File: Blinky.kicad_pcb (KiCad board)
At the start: 2 copper layers, 170 x 83.6 mm, 42 parts, among them J1 DTF13-4P-G003, J2 DTF13-4P-G003, J3 1053091104, J4 2002411132, Q1 IPD90P03P404ATMA2, Q2 IPD90P03P404ATMA2, U1 DCM4623TD2J13D0T00, U2 DCM4623TD2J13D0T00, U3 TLP184, U4 LTV-817S

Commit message: Finished layout rev 1
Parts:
- F1, F2: value 0031.8201 -> 0031.8221; footprint Fuse:Fuseholder_Cylinder-5x20mm_Schurter_0031_8201_Horizontal_Open -> AERO_Fuses:Schurter 0031.8221
- moved D1 27.6 mm to (210.0, 79.4), turned to 90 degrees
- moved R1 27.4 mm to (213.7, 79.5), turned to 90 degrees
- moved R2 27.1 mm to (218.0, 107.8)
- moved D2 26.8 mm to (218.0, 104.3)
- moved F1 14.1 mm to (75.0, 108.6)
- moved F2 14.1 mm to (75.0, 72.0)
- moved R6 12.6 mm to (88.8, 59.4)
- moved C3 7.06 mm to (186.7, 114.6), turned to 90 degrees
- moved L4 6.00 mm to (198.2, 67.0)
- moved R8 6.00 mm to (198.2, 59.8)
- moved C6 5.41 mm to (186.7, 70.5)
- moved L3 4.84 mm to (88.8, 68.2)
- moved R11 3.70 mm to (155.7, 102.9)
- moved R9 3.60 mm to (155.8, 98.4), turned to -90 degrees
- moved C4 3.20 mm to (112.2, 62.9)
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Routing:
- net /Control Signals/INVERTER-: track 0.00 -> 247.3 mm, vias 0 -> 3
- net /Control Signals/HV_FAULT: track 0.00 -> 133.0 mm
- net /Control Signals/HV_EN: track 0.00 -> 129.4 mm
- net /Control Signals/~{LV_FAULT}: track 0.00 -> 57.5 mm, vias 0 -> 1
- net TSMS12V: track 0.00 -> 55.7 mm, vias 0 -> 1
- net /Control Signals/LV_EN: track 0.00 -> 53.2 mm, vias 0 -> 1
- net /VICOR-1/HV_TRIM: track 0.00 -> 32.8 mm, vias 0 -> 1
- net /VICOR-2/HV_TRIM: track 0.00 -> 31.2 mm
- net /TSV Connectors/INVERTER+: track 0.00 -> 30.1 mm, vias 0 -> 10
- net /VICOR-2/VICOR_RAW: track 18.9 -> 0.00 mm
- net /VICOR-1/VICOR_RAW: track 18.9 -> 0.00 mm
- net Net-(D3-A): track 0.00 -> 10.1 mm
- net Net-(D2-A): track 0.00 -> 9.55 mm, vias 0 -> 1
- net Net-(D1-A): track 0.00 -> 8.61 mm, vias 0 -> 1
- net Net-(R11-Pad1): track 0.00 -> 8.56 mm
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- added copper zone on F.Cu, net /GLV Connectors/VICOR_FILTERED
- added copper zone on F.Cu, net /GLV Connectors/VICOR_OUT
- added copper zone on B.Cu, net /TSV Connectors/INVERTER+
- added copper zone on F.Cu, net /TSV Connectors/INVERTER+
- added copper zone on F.Cu, net /VICOR-1/VICOR_IN
- added copper zone on F.Cu, net /VICOR-1/VICOR_RAW
- added copper zone on F.Cu, net /VICOR-2/VICOR_IN
- added copper zone on F.Cu, net /VICOR-2/VICOR_RAW
- added copper zone on B.Cu, net LV_GND
- added copper zone on F.Cu, net LV_GND
- added copper zone on In1.Cu, net LV_GND
- added copper zone on In2.Cu, net LV_GND
- added copper zone on F.Cu, net Net-(F1-Pad2)
- added copper zone on F.Cu, net Net-(F2-Pad2)
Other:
- copper layers 2 -> 4

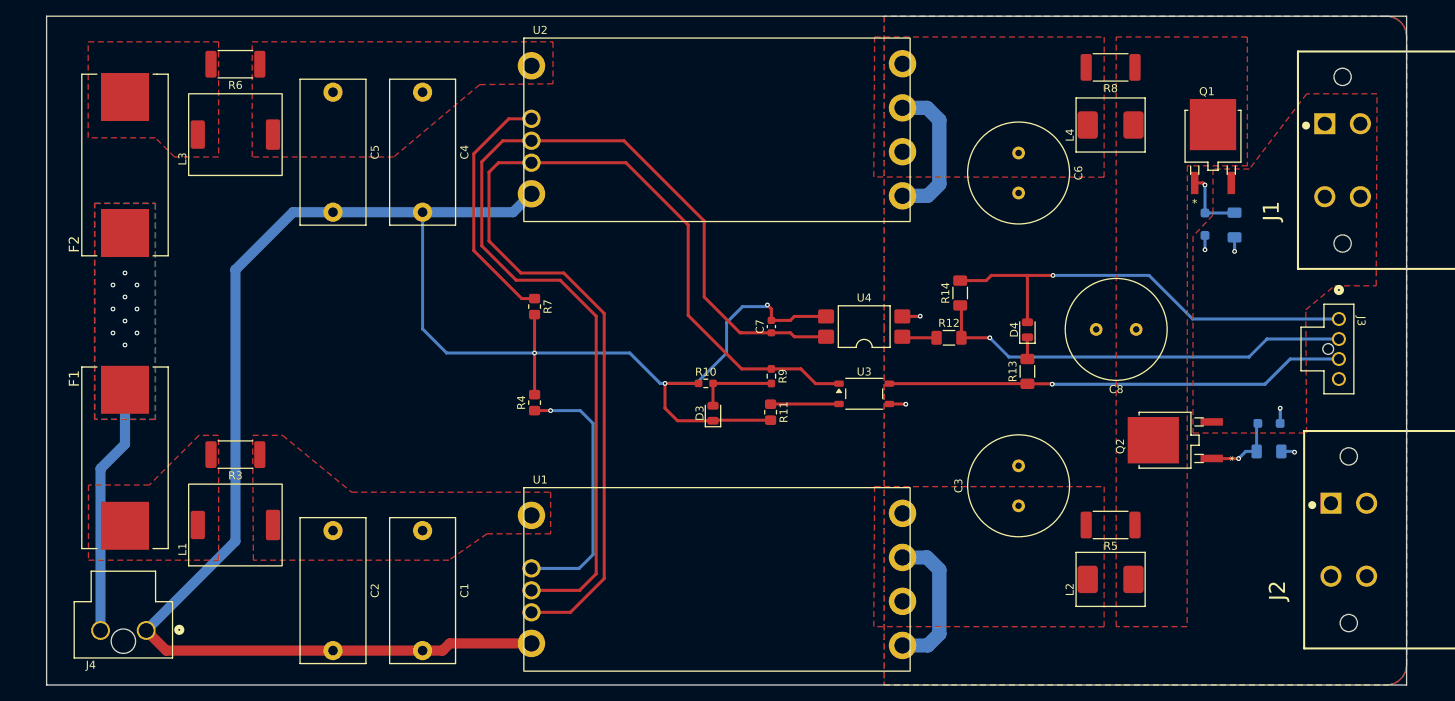
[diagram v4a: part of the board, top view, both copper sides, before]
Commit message: Routing and clearance changes. Added board cutouts and mounting holes
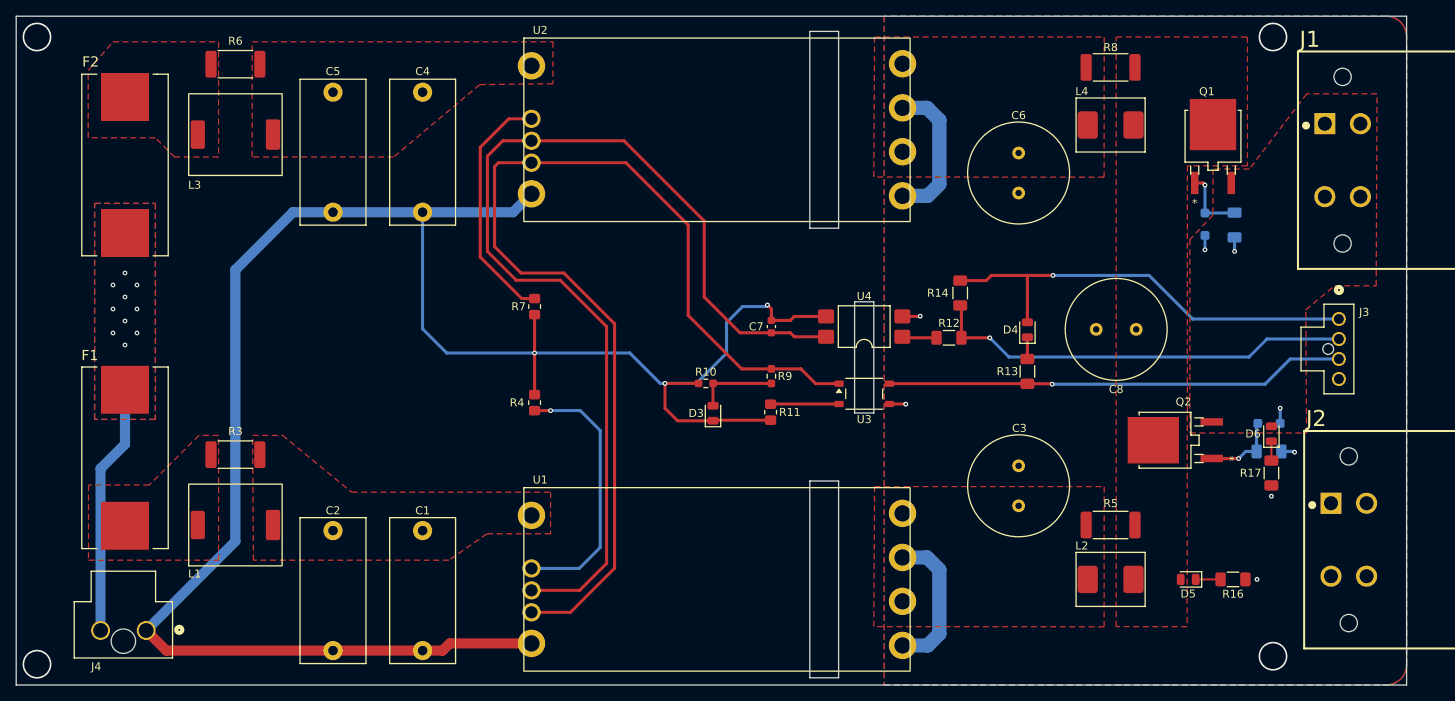
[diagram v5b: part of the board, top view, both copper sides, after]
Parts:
- added D5: LTST-C171KRKT, LED_SMD:LED_0805_2012Metric, F.Cu at (207.9, 123.8)
- added D6: LTST-C171KRKT, LED_SMD:LED_0805_2012Metric, F.Cu at (218.3, 105.6)
- added R16: 500, Resistor_SMD:R_1206_3216Metric_Pad1.30x1.75mm_HandSolder, F.Cu at (213.5, 123.8)
- added R17: 500, Resistor_SMD:R_1206_3216Metric_Pad1.30x1.75mm_HandSolder, F.Cu at (218.3, 110.5)
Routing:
- net Net-(D5-K): track 0.00 -> 3.11 mm
- net Net-(D6-K): track 0.00 -> 2.41 mm
- net /VICOR-1/HV_TRIM: track 32.8 -> 33.5 mm
- net /VICOR-2/HV_TRIM: track 31.2 -> 30.5 mm
- net LV_GND: vias 4 -> 8
- net (no net): vias 0 -> 2
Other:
- board size 170 x 83.6 mm -> 173.8 x 83.6 mm
